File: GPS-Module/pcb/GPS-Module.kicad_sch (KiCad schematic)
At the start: 0 parts

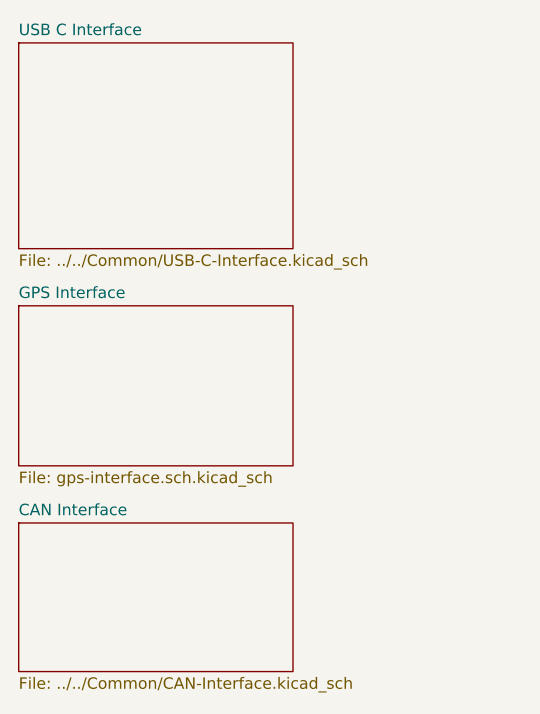
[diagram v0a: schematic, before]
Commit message: Deleted Can interface from Radio Module
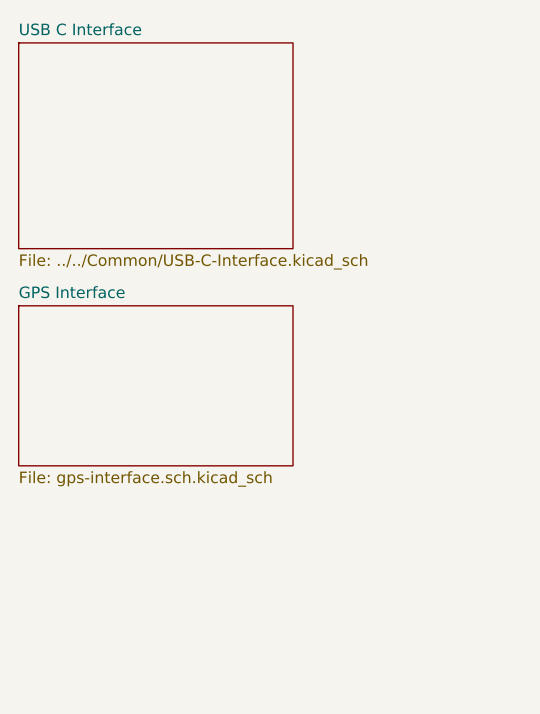
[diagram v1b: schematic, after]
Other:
- removed sheet CAN Interface
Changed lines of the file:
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@@
-	)
-	(sheet
-		(at 35.56 135.89)
-		(size 30.48 16.51)
-		(fields_autoplaced yes)
-		(stroke
-			(width 0.1524)
-			(type solid)
-		)
-		(fill
-			(color 0 0 0 0.0000)
-		)
-		(property "Sheetname" "CAN Interface"
-			(at 35.56 135.1784 0)
-			(effects
-				(font
-					(size 1.27 1.27)
-				)
-				(justify left bottom)
-			)
-		)
-		(property "Sheetfile" "../../Common/CAN-Interface.kicad_sch"
-			(at 35.56 152.9846 0)
-			(effects
-				(font
-					(size 1.27 1.27)
-				)
-				(justify left top)
-			)
-		)
-		(instances
-			(project "GPS-Module"
-				(path "/acc63f22-7eb8-450a-9af4-da5f4b8157d9"
-					(page "4")
-				)
-			)
-		)
 	)
 	(sheet
